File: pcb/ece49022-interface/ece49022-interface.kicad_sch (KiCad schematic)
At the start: 15 parts, among them J1 Conn_01x03_Pin, J2 Conn_01x05_Pin, J3 Conn_01x04_Pin, J4 Conn_01x04_Pin, J5 Conn_01x02_Pin, J6 Conn_01x02_Pin

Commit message: prepared for fill
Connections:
- net GPIO18: now also J1.3 (Pin_3)
- net GPIO22: no longer J1.3 (Pin_3)
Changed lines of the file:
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@@
 		)
 	)
-	(label "GPIO18"
+	(label "GPIO22"
 		(at 18.415 93.98 0)
 		(effects
@@
 		)
 	)
-	(label "GPIO22"
+	(label "GPIO18"
 		(at 102.235 65.405 0)
 		(effects

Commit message: final layout i think
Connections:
- net at R6.2: now also A1.11 (GPIO8); no longer A1.6 (GPIO4)
- net at A1.10 (GPIO7): now also R5.2
- net at A1.4 (GPIO2): no longer R4.2
- net at A1.5 (GPIO3): no longer R5.2
- net at A1.9 (GPIO6): now also R4.2
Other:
- moved on the sheet: H1, H2, H3, H4
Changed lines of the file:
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@@
+	(wire
+		(pts
+			(xy 109.22 153.67) (xy 122.555 153.67)
+		)
+		(stroke
+			(width 0)
+			(type default)
+		)
+	)
 	(wire
 		(pts
@@
 	(wire
 		(pts
+			(xy 122.555 148.59) (xy 114.3 148.59)
+		)
+		(stroke
+			(width 0)
+			(type default)
+		)
+	)
+	(wire
+		(pts
 			(xy 48.26 29.21) (xy 59.69 29.21)
 		)
@@
 	(wire
 		(pts
+			(xy 103.505 143.51) (xy 109.22 143.51)
+		)
+		(stroke
+			(width 0)
+			(type default)
+		)
+	)
+	(wire
+		(pts
 			(xy 191.135 53.975) (xy 191.135 55.245)
 		)
@@
 	(wire
 		(pts
-			(xy 103.505 143.51) (xy 122.555 143.51)
-		)
-		(stroke
-			(width 0)
-			(type default)
-		)
-	)
-	(wire
-		(pts
 			(xy 71.755 158.115) (xy 71.755 160.655)
 		)
@@
 	(wire
 		(pts
+			(xy 111.76 140.97) (xy 111.76 151.13)
+		)
+		(stroke
+			(width 0)
+			(type default)
+		)
+	)
+	(wire
+		(pts
+			(xy 114.3 138.43) (xy 114.3 148.59)
+		)
+		(stroke
+			(width 0)
+			(type default)
+		)
+	)
+	(wire
+		(pts
 			(xy 99.06 60.325) (xy 123.19 60.325)
 		)
@@
 	(wire
 		(pts
+			(xy 111.76 151.13) (xy 122.555 151.13)
+		)
+		(stroke
+			(width 0)
+			(type default)
+		)
+	)
+	(wire
+		(pts
 			(xy 118.11 47.625) (xy 118.11 50.165)
 		)
@@
 	(wire
 		(pts
-			(xy 103.505 138.43) (xy 122.555 138.43)
-		)
-		(stroke
-			(width 0)
-			(type default)
-		)
-	)
-	(wire
-		(pts
 			(xy 168.275 148.59) (xy 178.435 148.59)
 		)
@@
 	(wire
 		(pts
+			(xy 109.22 143.51) (xy 109.22 153.67)
+		)
+		(stroke
+			(width 0)
+			(type default)
+		)
+	)
+	(wire
+		(pts
 			(xy 248.285 137.795) (xy 248.285 139.065)
 		)
@@
 	(wire
 		(pts
+			(xy 103.505 138.43) (xy 114.3 138.43)
+		)
+		(stroke
+			(width 0)
+			(type default)
+		)
+	)
+	(wire
+		(pts
 			(xy 86.36 156.21) (xy 97.79 156.21)
 		)
@@
 	(wire
 		(pts
-			(xy 91.44 140.97) (xy 122.555 140.97)
-		)
-		(stroke
-			(width 0)
-			(type default)
-		)
-	)
-	(wire
-		(pts
 			(xy 183.515 72.39) (xy 203.835 72.39)
 		)
@@
 		(pts
 			(xy 61.595 160.655) (xy 71.755 160.655)
+		)
+		(stroke
+			(width 0)
+			(type default)
+		)
+	)
+	(wire
+		(pts
+			(xy 91.44 140.97) (xy 111.76 140.97)
 		)
 		(stroke
@@
 	(symbol
 		(lib_id "Mechanical:MountingHole")
-		(at 238.76 46.99 0)
+		(at 247.65 21.59 0)
 		(unit 1)
 		(exclude_from_sim no)
@@
 		(dnp no)
 		(property "Reference" "H1"
-			(at 241.3 45.8216 0)
+			(at 250.19 20.4216 0)
 			(effects
 				(font
@@
 		)
 		(property "Value" "MountingHole"
-			(at 241.3 48.133 0)
+			(at 250.19 22.733 0)
 			(effects
 				(font
@@
 		)
 		(property "Footprint" "MountingHole:MountingHole_2.7mm_M2.5"
-			(at 238.76 46.99 0)
+			(at 247.65 21.59 0)
 			(effects
 				(font
@@
 		)
 		(property "Datasheet" "~"
-			(at 238.76 46.99 0)
+			(at 247.65 21.59 0)
 			(effects
 				(font
@@
 		)
 		(property "Description" ""
-			(at 238.76 46.99 0)
+			(at 247.65 21.59 0)
 			(effects
 				(font
@@
 	(symbol
 		(lib_id "Mechanical:MountingHole")
-		(at 259.08 60.96 0)
+		(at 267.97 35.56 0)
 		(unit 1)
 		(exclude_from_sim no)
@@
 		(dnp no)
 		(property "Reference" "H3"
-			(at 261.62 59.7916 0)
+			(at 270.51 34.3916 0)
 			(effects
 				(font
@@
 		)
 		(property "Value" "MountingHole"
-			(at 261.62 62.103 0)
+			(at 270.51 36.703 0)
 			(effects
 				(font
@@
 		)
 		(property "Footprint" "MountingHole:MountingHole_2.7mm_M2.5"
-			(at 259.08 60.96 0)
+			(at 267.97 35.56 0)
 			(effects
 				(font
@@
 		)
 		(property "Datasheet" "~"
-			(at 259.08 60.96 0)
+			(at 267.97 35.56 0)
 			(effects
 				(font
@@
 		)
 		(property "Description" ""
-			(at 259.08 60.96 0)
+			(at 267.97 35.56 0)
 			(effects
 				(font
@@
 	(symbol
 		(lib_id "Mechanical:MountingHole")
-		(at 238.76 60.96 0)
+		(at 247.65 35.56 0)
 		(unit 1)
 		(exclude_from_sim no)
@@
 		(dnp no)
 		(property "Reference" "H4"
-			(at 241.3 59.7916 0)
+			(at 250.19 34.3916 0)
 			(effects
 				(font
@@
 		)
 		(property "Value" "MountingHole"
-			(at 241.3 62.103 0)
+			(at 250.19 36.703 0)
 			(effects
 				(font
@@
 		)
 		(property "Footprint" "MountingHole:MountingHole_2.7mm_M2.5"
-			(at 238.76 60.96 0)
+			(at 247.65 35.56 0)
 			(effects
 				(font
@@
 		)
 		(property "Datasheet" "~"
-			(at 238.76 60.96 0)
+			(at 247.65 35.56 0)
 			(effects
 				(font
@@
 		)
 		(property "Description" ""
-			(at 238.76 60.96 0)
+			(at 247.65 35.56 0)
 			(effects
 				(font
@@
 	(symbol
 		(lib_id "Mechanical:MountingHole")
-		(at 259.08 46.99 0)
+		(at 267.97 21.59 0)
 		(unit 1)
 		(exclude_from_sim no)
@@
 		(dnp no)
 		(property "Reference" "H2"
-			(at 261.62 45.8216 0)
+			(at 270.51 20.4216 0)
 			(effects
 				(font
@@
 		)
 		(property "Value" "MountingHole"
-			(at 261.62 48.133 0)
+			(at 270.51 22.733 0)
 			(effects
 				(font
@@
 		)
 		(property "Footprint" "MountingHole:MountingHole_2.7mm_M2.5"
-			(at 259.08 46.99 0)
+			(at 267.97 21.59 0)
 			(effects
 				(font
@@
 		)
 		(property "Datasheet" "~"
-			(at 259.08 46.99 0)
+			(at 267.97 21.59 0)
 			(effects
 				(font
@@
 		)
 		(property "Description" ""
-			(at 259.08 46.99 0)
-			(effects
-				(font
+			(at 267.97 21.59 0)
+			(effects
+				(font

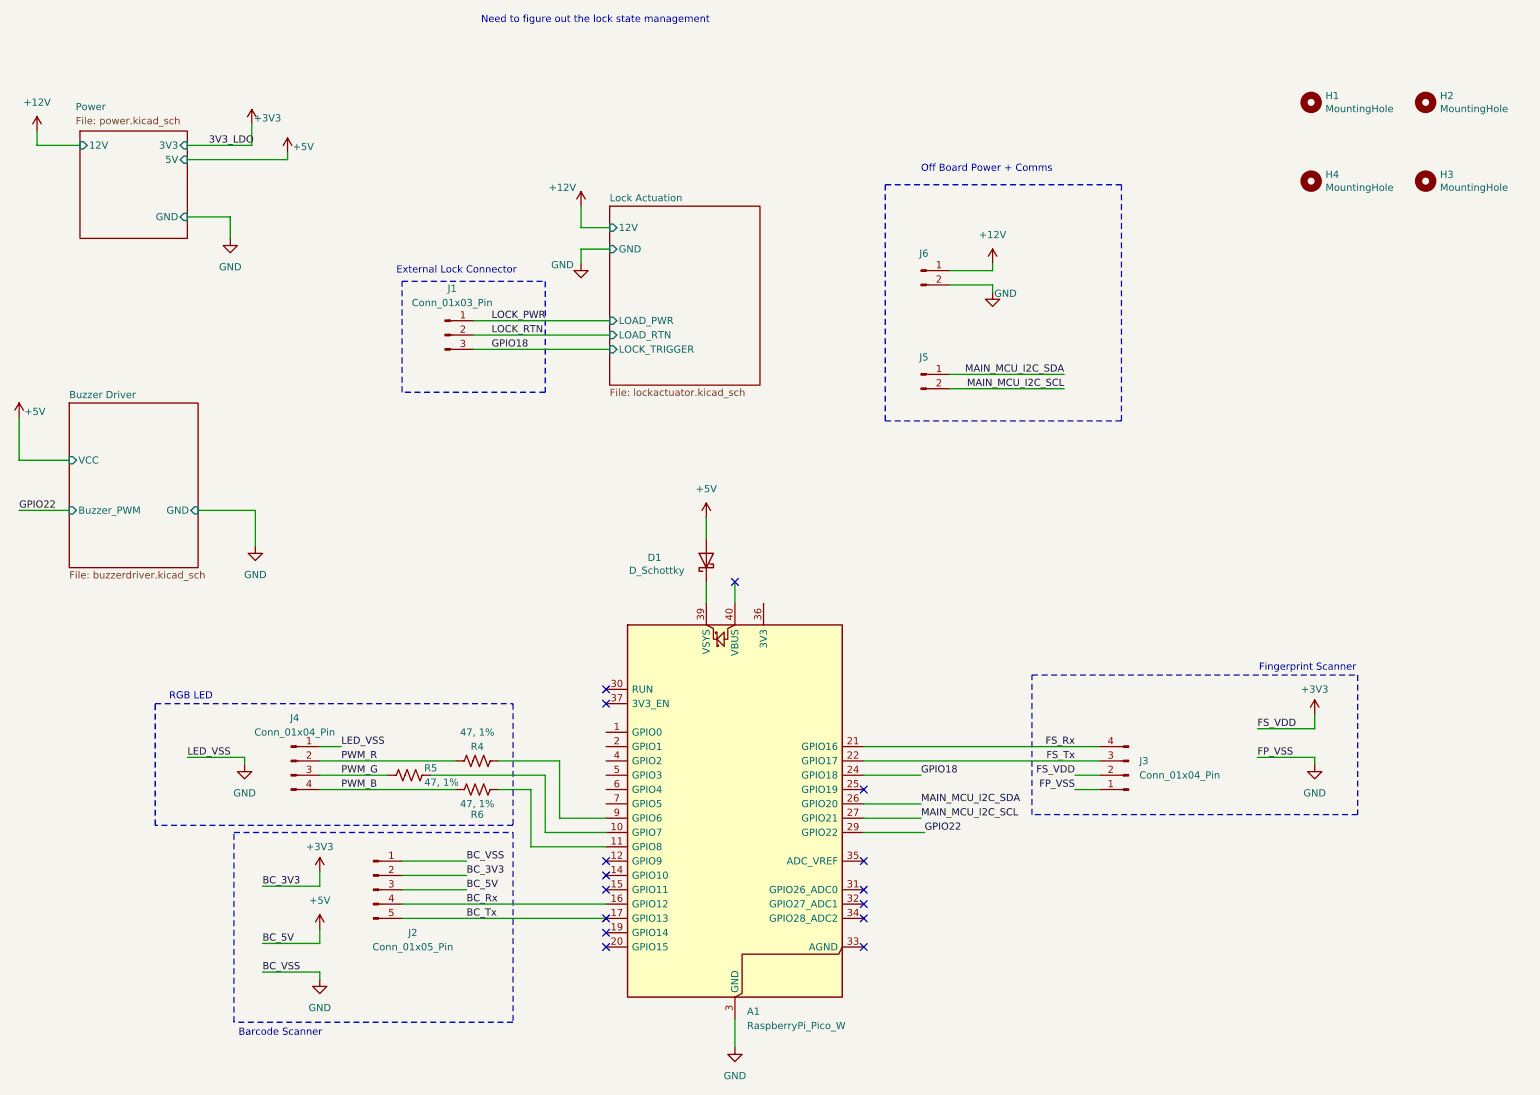
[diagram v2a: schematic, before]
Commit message: need to add traces
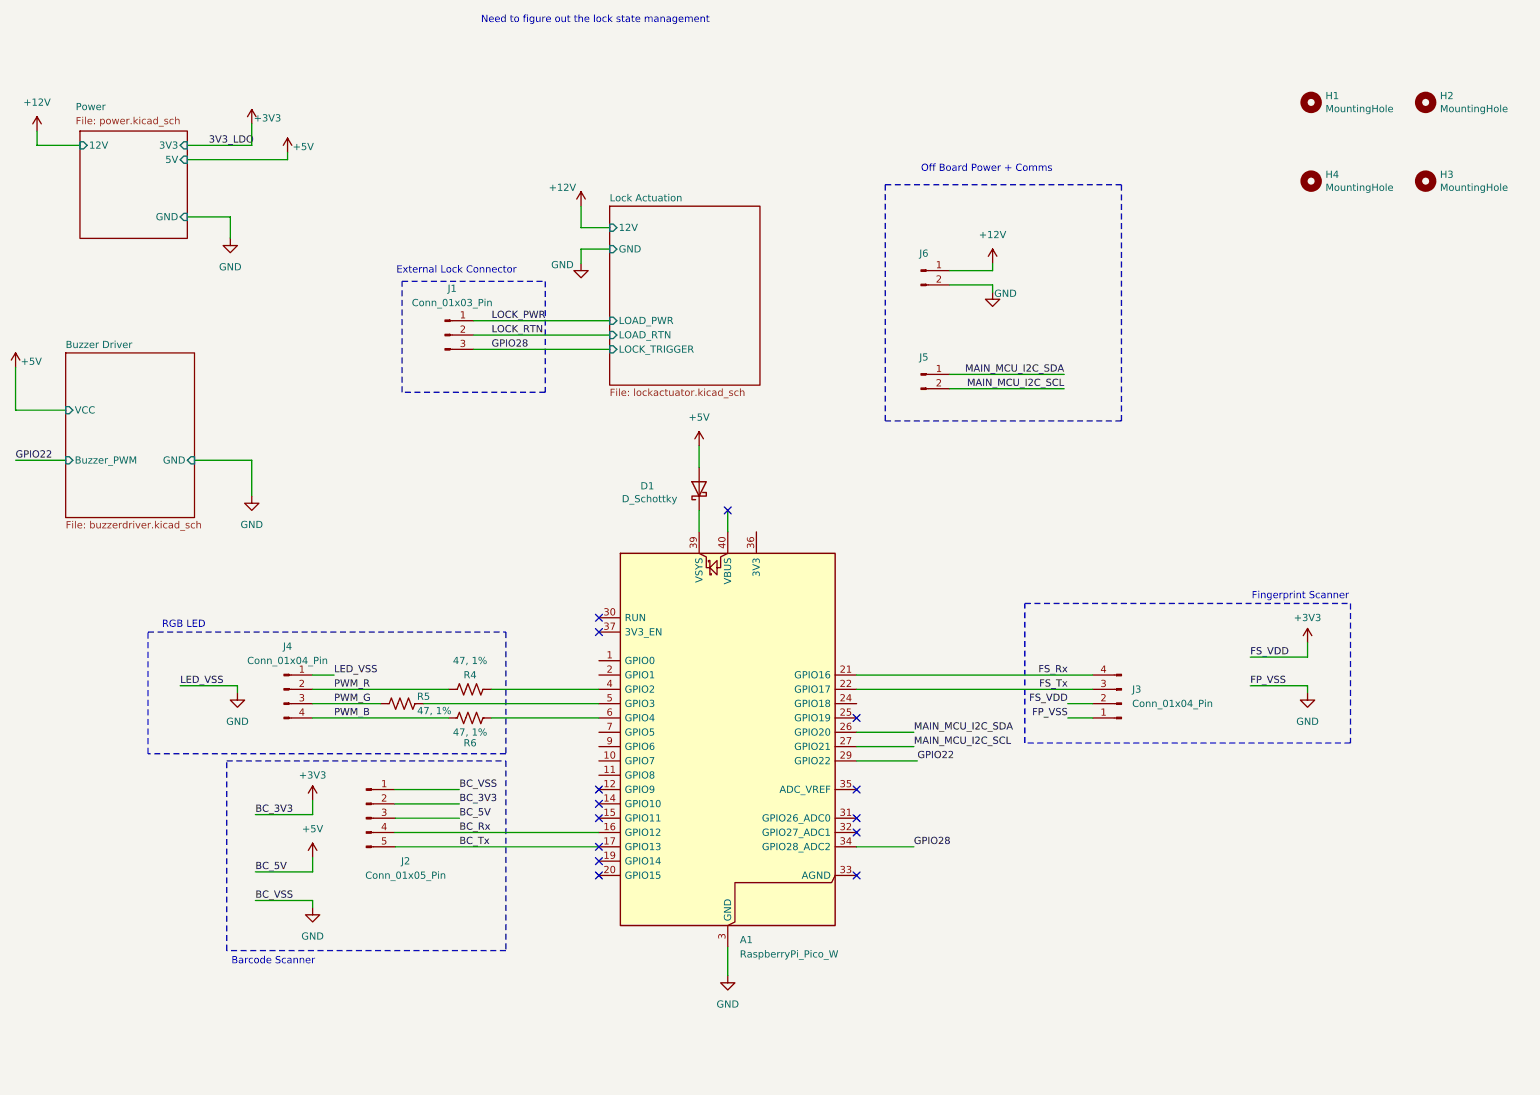
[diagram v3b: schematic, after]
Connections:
- net at R6.2: now also A1.6 (GPIO4); no longer A1.11 (GPIO8)
- net at A1.10 (GPIO7): no longer R5.2
- net GPIO28: now reaches A1.34 (GPIO28_ADC2)
- net GPIO28: now also J1.3 (Pin_3)
- net at A1.4 (GPIO2): now also R4.2
- net at A1.5 (GPIO3): now also R5.2
- net at A1.9 (GPIO6): no longer R4.2
- net GPIO18: no longer names the net of A1.24 (GPIO18)
- net GPIO18: no longer J1.3 (Pin_3)
- no-connect marks 15 -> 14
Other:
- moved on the sheet: A1, D1, J2, J3, J4, R4, R5, R6

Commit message: update
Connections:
- net BC_Rx: now also A1.11 (GPIO8); no longer A1.16 (GPIO12)
- net BC_Tx: now also A1.12 (GPIO9); no longer A1.17 (GPIO13)
- no-connect marks 14 -> 12
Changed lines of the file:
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@@
-	)
-	(no_connect
-		(at 121.285 153.67)
 	)
 	(no_connect
@@
 	)
 	(no_connect
-		(at 121.285 143.51)
-	)
-	(no_connect
 		(at 121.285 113.03)
 	)
@@
 	(wire
 		(pts
+			(xy 109.855 140.97) (xy 121.285 140.97)
+		)
+		(stroke
+			(width 0)
+			(type default)
+		)
+	)
+	(wire
+		(pts
 			(xy 70.485 155.575) (xy 70.485 158.115)
 		)
@@
 	(wire
 		(pts
-			(xy 85.09 151.13) (xy 121.285 151.13)
-		)
-		(stroke
-			(width 0)
-			(type default)
-		)
-	)
-	(wire
-		(pts
 			(xy 191.135 51.435) (xy 183.515 51.435)
 		)
@@
 	(wire
 		(pts
+			(xy 85.09 153.67) (xy 115.57 153.67)
+		)
+		(stroke
+			(width 0)
+			(type default)
+		)
+	)
+	(wire
+		(pts
 			(xy 102.235 130.81) (xy 121.285 130.81)
 		)
@@
 	(wire
 		(pts
+			(xy 115.57 153.67) (xy 115.57 143.51)
+		)
+		(stroke
+			(width 0)
+			(type default)
+		)
+	)
+	(wire
+		(pts
 			(xy 60.325 163.195) (xy 70.485 163.195)
 		)
@@
 	(wire
 		(pts
+			(xy 115.57 143.51) (xy 121.285 143.51)
+		)
+		(stroke
+			(width 0)
+			(type default)
+		)
+	)
+	(wire
+		(pts
 			(xy 204.47 128.27) (xy 208.915 128.27)
 		)
@@
 	(wire
 		(pts
+			(xy 85.09 151.13) (xy 109.855 151.13)
+		)
+		(stroke
+			(width 0)
+			(type default)
+		)
+	)
+	(wire
+		(pts
 			(xy 167.005 138.43) (xy 177.8 138.43)
 		)
@@
 	(wire
 		(pts
+			(xy 109.855 151.13) (xy 109.855 140.97)
+		)
+		(stroke
+			(width 0)
+			(type default)
+		)
+	)
+	(wire
+		(pts
 			(xy 144.145 171.45) (xy 144.145 176.53)
 		)
@@
 		)
 		(stroke
-			(width 0)
-			(type default)
-		)
-	)
-	(wire
-		(pts
-			(xy 85.09 153.67) (xy 121.285 153.67)
-		)
-		(stroke

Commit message: Initial PCB
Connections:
- net +3V3: now also A1.36 (3V3)
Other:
- sheet Power ports: added none; removed 3V3
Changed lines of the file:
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@@
 	(wire
 		(pts
-			(xy 59.69 25.4) (xy 59.69 29.21)
-		)
-		(stroke
-			(width 0)
-			(type default)
-		)
-	)
-	(wire
-		(pts
 			(xy 17.78 76.2) (xy 26.67 76.2)
 		)
@@
 	(wire
 		(pts
-			(xy 48.26 29.21) (xy 59.69 29.21)
+			(xy 70.485 130.81) (xy 94.615 130.81)
 		)
 		(stroke
@@
 	(wire
 		(pts
-			(xy 70.485 130.81) (xy 94.615 130.81)
+			(xy 48.26 31.75) (xy 66.04 31.75)
 		)
 		(stroke
@@
 	(wire
 		(pts
-			(xy 48.26 31.75) (xy 66.04 31.75)
+			(xy 144.145 93.98) (xy 144.145 97.79)
 		)
 		(stroke
@@
 	(wire
 		(pts
-			(xy 144.145 93.98) (xy 144.145 97.79)
+			(xy 85.09 153.67) (xy 115.57 153.67)
 		)
 		(stroke
@@
 	(wire
 		(pts
-			(xy 85.09 153.67) (xy 115.57 153.67)
+			(xy 102.235 130.81) (xy 121.285 130.81)
 		)
 		(stroke
@@
 	(wire
 		(pts
-			(xy 102.235 130.81) (xy 121.285 130.81)
+			(xy 191.135 53.975) (xy 191.135 55.245)
 		)
 		(stroke
@@
 	(wire
 		(pts
-			(xy 191.135 53.975) (xy 191.135 55.245)
+			(xy 70.485 145.415) (xy 70.485 147.955)
 		)
 		(stroke
@@
 	(wire
 		(pts
-			(xy 70.485 145.415) (xy 70.485 147.955)
+			(xy 149.225 82.55) (xy 149.225 97.79)
 		)
 		(stroke
@@
 		)
 	)
-	(label "3V3_LDO"
-		(at 52.07 29.21 0)
-		(effects
-			(font
-				(size 1.27 1.27)
-			)
-			(justify left bottom)
-		)
-	)
 	(label "BC_VSS"
 		(at 96.52 143.51 0)
@@
 	(symbol
 		(lib_id "power:+3V3")
-		(at 59.69 25.4 0)
+		(at 149.225 82.55 0)
 		(unit 1)
 		(exclude_from_sim no)
@@
 		(dnp no)
 		(property "Reference" "#PWR018"
-			(at 59.69 29.21 0)
+			(at 149.225 86.36 0)
 			(effects
 				(font
@@
 		)
 		(property "Value" "+3V3"
-			(at 62.484 24.384 0)
+			(at 149.225 77.47 0)
 			(effects
 				(font
@@
 		)
 		(property "Footprint" ""
-			(at 59.69 25.4 0)
+			(at 149.225 82.55 0)
 			(effects
 				(font
@@
 		)
 		(property "Datasheet" ""
-			(at 59.69 25.4 0)
+			(at 149.225 82.55 0)
 			(effects
 				(font
@@
 		)
 		(property "Description" "Power symbol creates a global label with name \"+3V3\""
-			(at 59.69 25.4 0)
+			(at 149.225 82.55 0)
 			(effects
 				(font
@@
 			)
 		)
-		(pin "3V3" input
-			(at 48.26 29.21 0)
-			(effects
-				(font
-					(size 1.27 1.27)
-				)
-				(justify right)
-			)
-		)

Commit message: done? i think
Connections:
- net BC_Rx: now also A1.6 (GPIO4); no longer A1.11 (GPIO8)
- net BC_Tx: now also A1.7 (GPIO5); no longer A1.12 (GPIO9)
- net GPIO28: no longer A1.34 (GPIO28_ADC2)
- net at R6.2: now also A1.31 (GPIO26_ADC0); no longer A1.6 (GPIO4)
- net at A1.32 (GPIO27_ADC1): now also R5.2
- net at R4.2: now also A1.34 (GPIO28_ADC2); no longer A1.4 (GPIO2)
- net at A1.5 (GPIO3): no longer R5.2
- no-connect marks 12 -> 8
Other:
- moved on the sheet: J2, J4, R4, R5, R6

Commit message: done?
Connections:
- net GPIO28 is gone; now on net GPIO13: J1.3 (Pin_3)
- net GPIO13: now reaches A1.17 (GPIO13)
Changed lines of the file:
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@@
+	(wire
+		(pts
+			(xy 114.3 153.67) (xy 121.285 153.67)
+		)
+		(stroke
+			(width 0)
+			(type default)
+		)
+	)
 	(wire
 		(pts
@@
 		)
 	)
-	(label "GPIO28"
+	(label "GPIO13"
 		(at 102.235 65.405 0)
 		(effects
@@
 		)
 	)
-	(label "GPIO28"
-		(at 67.31 184.785 0)
-		(effects
-			(font
+	(label "GPIO13"
+		(at 114.3 153.67 0)
+		(effects
+			(font

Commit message: need to finish power
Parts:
- removed J5: Conn_01x02_Pin, Connector_PinHeader_2.54mm:PinHeader_1x02_P2.54mm_Vertical, symbol Connector:Conn_01x02_Pin
- added J5: Conn_01x08_Pin, Connector_PinHeader_2.54mm:PinHeader_1x08_P2.54mm_Vertical, symbol Connector:Conn_01x08_Pin
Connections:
- net BC_Rx: now also J2.5 (Pin_5); no longer J2.4 (Pin_4)
- net BC_Tx: now also J2.4 (Pin_4); no longer J2.5 (Pin_5)
- net GPIO13: no longer A1.17 (GPIO13)
- net MAIN_MCU_I2C_SCL: now also A1.17 (GPIO13), J5.5 (Pin_5), J5.6 (Pin_6), J5.7 (Pin_7), J5.8 (Pin_8); no longer A1.27 (GPIO21)
- net MAIN_MCU_I2C_SDA: now also A1.16 (GPIO12), J5.1 (Pin_1), J5.2 (Pin_2), J5.3 (Pin_3), J5.4 (Pin_4); no longer A1.26 (GPIO20)
- net at R6.2: now also A1.5 (GPIO3); no longer A1.31 (GPIO26_ADC0)
- net GPIO10: now reaches A1.14 (GPIO10)
- net at A1.2 (GPIO1): now also R4.2
- net at A1.32 (GPIO27_ADC1): no longer R5.2
- net at A1.34 (GPIO28_ADC2): no longer R4.2
- net at A1.4 (GPIO2): now also R5.2
- net GPIO22: no longer names the net of A1.29 (GPIO22)
- no-connect marks 8 -> 7
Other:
- moved on the sheet: J2, J4, R4, R5, R6
